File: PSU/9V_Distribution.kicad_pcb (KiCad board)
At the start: 2 copper layers, 50 x 70 mm, 22 parts, among them J1 Screw_Terminal_2_P5.00mm, J2 Screw_Terminal_2_P5.00mm, J3 Screw_Terminal_2_P5.00mm, J4 Screw_Terminal_2_P5.00mm, U4 LM2596S-5

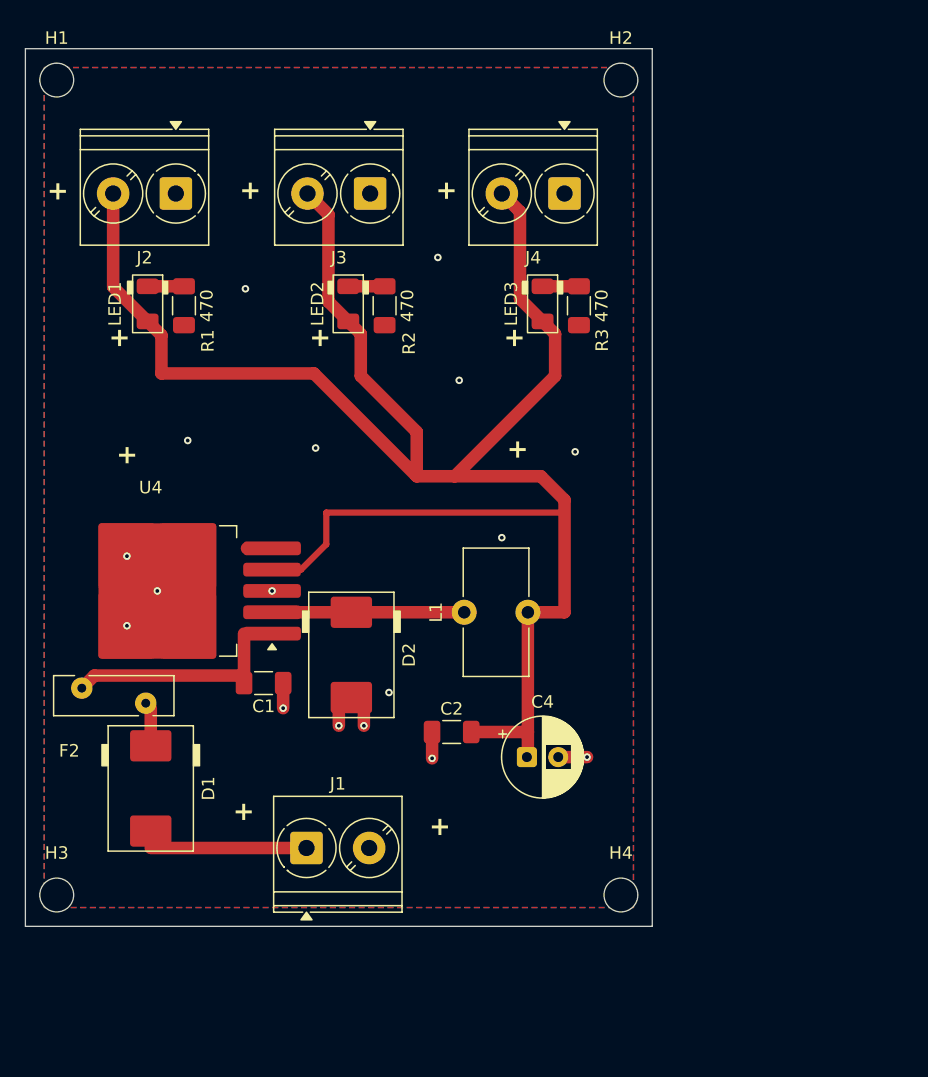
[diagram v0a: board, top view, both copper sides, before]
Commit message: Add the mainboard 9V branch to the PSU
Second, independent regulator on the PSU so the mainboard does not share a
rail with the PWM-switched backlighting. Tapped from D1's cathode: the
reverse protection is shared, the fuse is not, so a fault on one branch
does not take down the other.

  F3  0.5A polyfuse, mainboard branch only
  U1  P78A05-1000, the same module already used on RMP V5
  C5/C6, C7/C8  100nF + 100uF each side, mirroring RMP V5
  J5  screw terminal, beside J1, so both cables leave the same edge

Nets are labelled VIN_MB and +5V_MB rather than left as Net-(U1-+VOUT).

Layout: the whole chain sits in the y 44..56 band, which was empty. That
band was empty of footprints but not of copper -- the buck's output
distribution ran through it to reach J2/J3/J4. That distribution now runs
on a spine above the band at y 44.8 and crosses to the bottom half through
a single 13mm bottom-layer link at x 144.5, well away from the switching
loop. Everything else stays on the front, so the ground plane keeps one
narrow slot and nothing more.

The 9V climbs the left edge in the 2mm corridor between the board edge and
U4's tab; the 5V descends the right edge to J5. C4 moved 1.5mm to clear
the terminal.

0 unconnected items, 0 schematic parity issues, no silkscreen violations.
DRC reports the stale ground pour until the zone is refilled in Pcbnew:
79 of the 95 violations name it, the other 16 are the pre-existing library
links.

Co-Authored-By: Claude Opus 5 <noreply@anthropic.com>
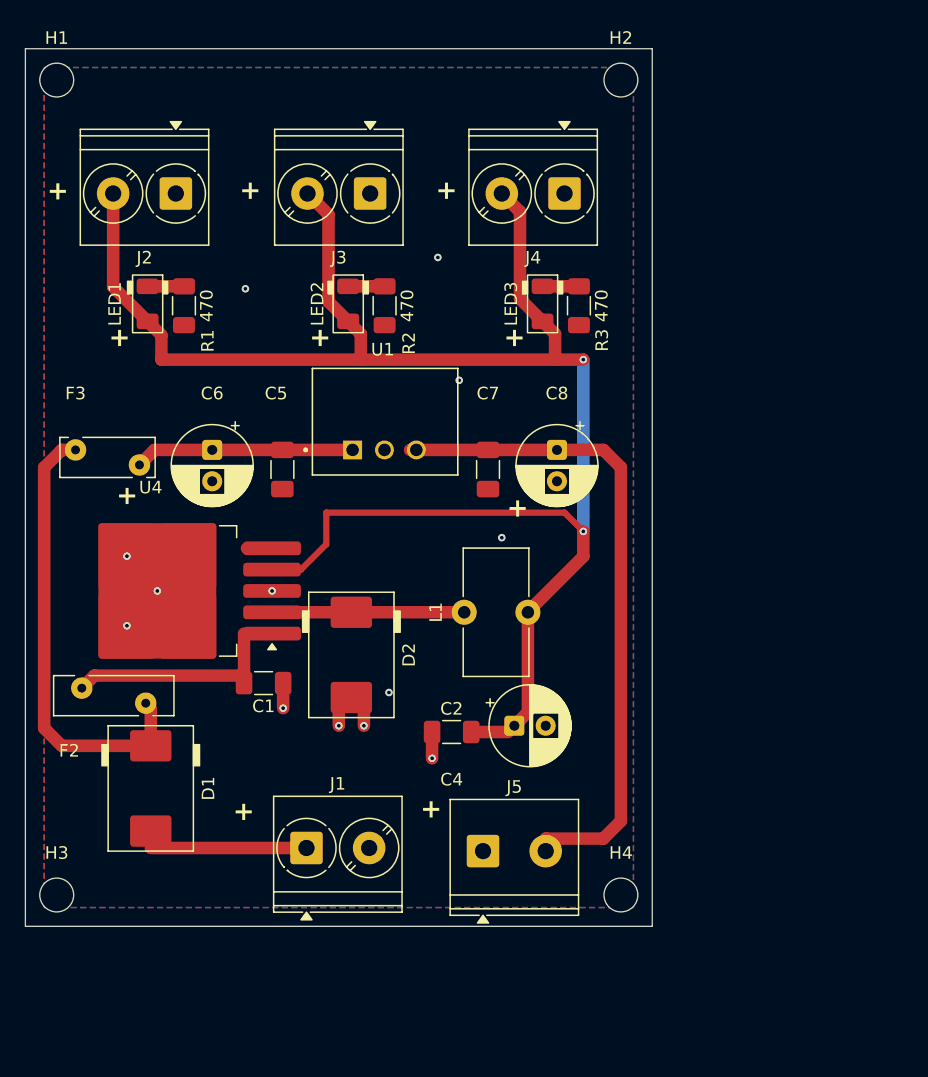
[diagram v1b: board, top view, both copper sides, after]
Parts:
- added C5: 100nF, Capacitor_SMD:C_1206_3216Metric_Pad1.33x1.80mm_HandSolder, F.Cu at (120.5, 53.6)
- added C6: 100uF, Capacitor_THT:CP_Radial_D6.3mm_P2.50mm, F.Cu at (114.9, 52.0)
- added C7: 100nF, Capacitor_SMD:C_1206_3216Metric_Pad1.33x1.80mm_HandSolder, F.Cu at (136.9, 53.6)
- added C8: 100uF, Capacitor_THT:CP_Radial_D6.3mm_P2.50mm, F.Cu at (142.4, 52.0)
- added F3: 0.5A, Fuse:Fuse_Bourns_MF-RHT050, F.Cu at (104.0, 52.0)
- added J5: Screw_Terminal_2_P5.00mm, TerminalBlock_Phoenix:TerminalBlock_Phoenix_PT-1,5-2-5.0-H_1x02_P5.00mm_Horizontal, F.Cu at (136.5, 84.0)
- added U1: P78A05-1000, Custom_Footprints:CONV_P78A05-1000, F.Cu at (126.1, 52.0)
- moved C4 2.69 mm to (139.0, 74.0)
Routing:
- net /+5V_MB: track 0.00 -> 53.2 mm
- net Net-(D1-K): track 3.00 -> 36.0 mm
- net Net-(LED1-A): track 160.7 -> 141.7 mm, vias 0 -> 2
- net /VIN_MB: track 0.00 -> 17.5 mm
- net GND: track 10.5 -> 8.20 mm, vias 17 -> 13

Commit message: Enlarge the PSU to 70x80 and move the mainboard branch into the new space
The board was 50x70 with one regulator; adding a second made it cramped
enough that parts were clearing each other by fractions of a millimetre and
the buck's output had to cross the new chain on the bottom layer.

Growing right and down to 70 x 80 keeps every existing coordinate, so the
buck section does not move. The P78A05 chain now runs vertically in the new
strip at x 150..170, which frees the middle band again: the buck's output
distribution is back to its original routing and the bottom-layer jumper is
gone. All 55 tracks are on the front and the ground plane is uncut.

Mounting holes move to a 65 x 75 pattern, so the printed base needs
reprinting. The 9 V reaches the new strip along the bottom edge at y 78,
between C4's pads and J1's courtyard.

Stitching vias restored in the middle band and added in the new area.

0 schematic parity issues. With the zone fill stripped, DRC finds no
clearance, crossing, short, hole or silkscreen violations; everything it
reports on the file as committed is either the stale pour (23) or the
pre-existing library links (16). Refill in Pcbnew with B.

Co-Authored-By: Claude Opus 5 <noreply@anthropic.com>
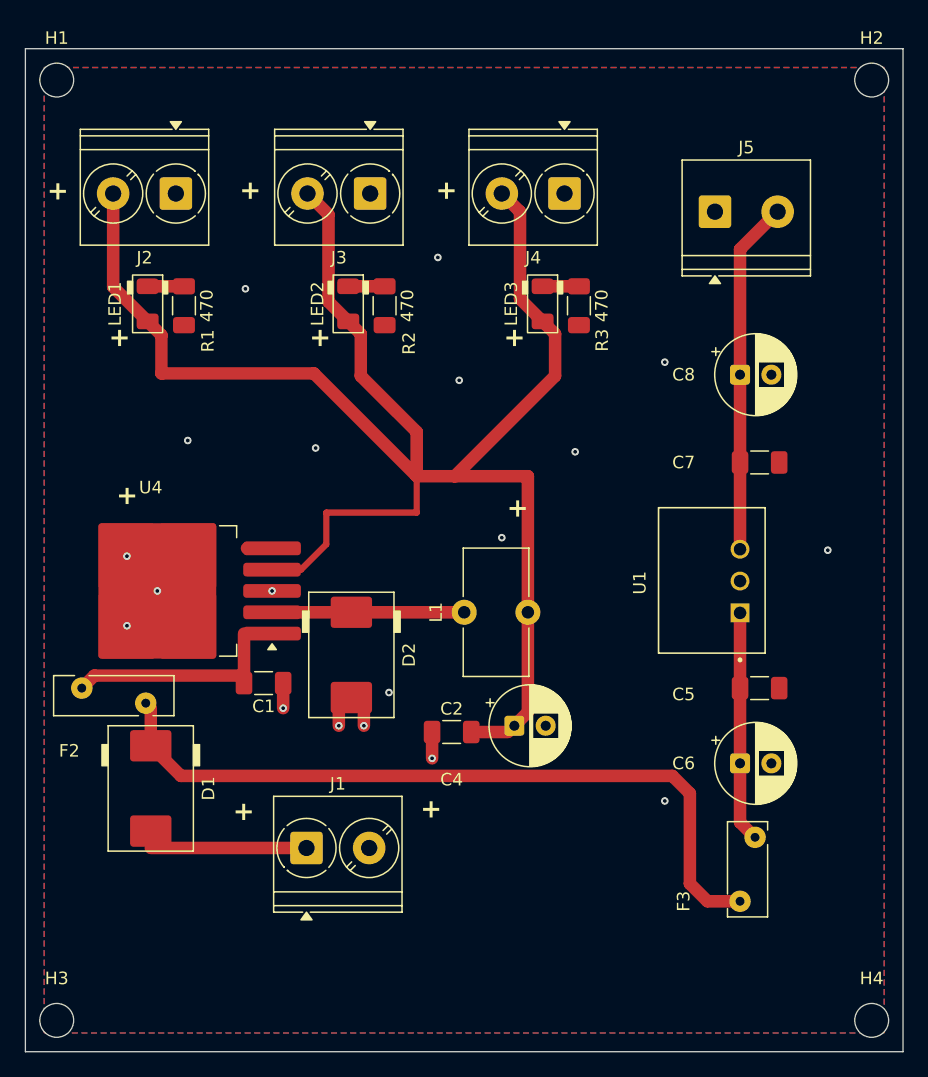
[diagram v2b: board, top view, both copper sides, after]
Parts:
- moved F3 64.1 mm to (157.0, 88.0), turned to 90 degrees
- moved J5 54.3 mm to (155.0, 33.0)
- moved C6 49.0 mm to (157.0, 77.0), turned to 0 degrees
- moved C5 41.9 mm to (158.6, 71.0), turned to 0 degrees
- moved U1 33.5 mm to (157.0, 65.0), turned to 90 degrees
- moved H4 22.4 mm to (167.5, 97.5)
- moved C7 21.7 mm to (158.6, 53.0), turned to 0 degrees
- moved H2 20.0 mm to (167.5, 22.5)
- moved C8 15.8 mm to (157.0, 46.0), turned to 0 degrees
- moved H3 10.0 mm to (102.5, 97.5)
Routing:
- net /+5V_MB: track 53.2 -> 28.2 mm
- net Net-(D1-K): track 36.0 -> 59.4 mm
- net Net-(LED1-A): track 141.7 -> 143.4 mm, vias 2 -> 0
- net /VIN_MB: track 17.5 -> 18.4 mm
- net GND: vias 13 -> 19
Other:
- board size 50 x 70 mm -> 70 x 80 mm

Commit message: Turn J5 round and move the PSU notes clear of the drawing
J5 was placed with its wire entry facing C8, leaving no room for the
cables. Rotated 180 and moved to (160, 33) so the cables leave over the
top edge, the same way J2-J4 do. The output track follows pad 2 to its new
position.

The two schematic notes sat on top of each other and over U1's fields.
They move below the drawing, which ends at y 127, and become four:
the two supply branches, the shared reverse protection with separate
fuses, what D2 is for, and C1's voltage rating. The old note claimed C2
needed 25 V as well; it does not, it sits on the 5 V output.

Includes the zone refill done in Pcbnew, which brought the board to 16
violations, all library links, with 0 unconnected and 0 parity issues.
Moving J5 makes the pour stale again for 8 of them, so it needs one more
refill.

Co-Authored-By: Claude Opus 5 <noreply@anthropic.com>
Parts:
- moved J5 5.00 mm to (160.0, 33.0), turned to 180 degrees

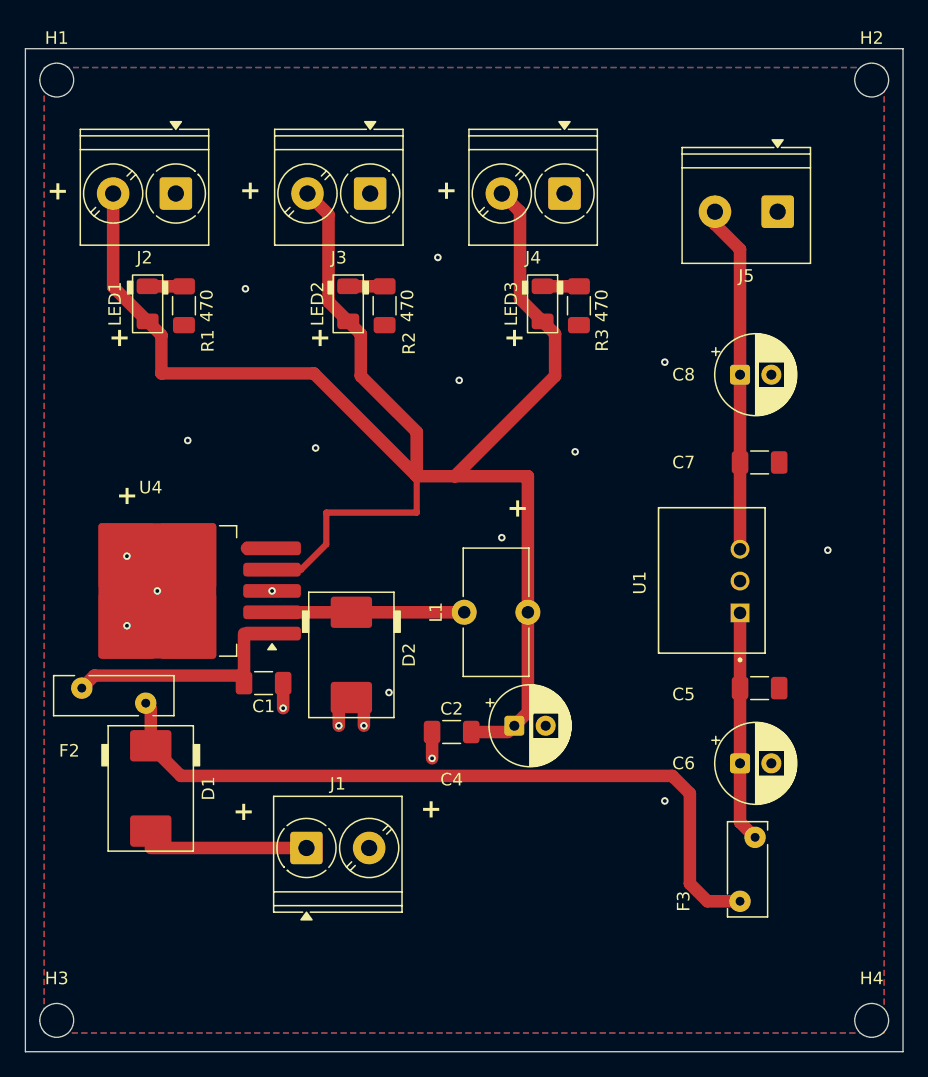
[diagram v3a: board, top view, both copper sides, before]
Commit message: Make the PSU buck section through-hole and give it room
D1, D2, C1 and C2 were SMD in among through-hole parts, for no better reason
than matching what the board already had. Two of the four conversions are
not about convenience:

  C1  sits across the 9V input and needs 25V of rating, which a 1206 MLCC of
      that capacitance does not come in. As an electrolytic the problem goes
      away instead of being documented.
  C2  is the buck's output capacitor and the LM2596 wants ESR there. As a
      ceramic it had none, which is why C4 exists; as an electrolytic it
      brings its own.

D1 and D2 become 1N5822 on the stock Device:D_Schottky symbol, which also
drops four missing-library warnings. Watch the polarity: the SS54 symbol has
pin 1 on the right and D_Schottky has it on the left, so both diodes are
rotated 180 to keep the cathode where it was -- the netlist confirms D1.2 on
the input, D2.1 on the switch node. D2 is mounted vertically on a 5.08mm
pitch, shorter than the SMC's 6.8mm, so the commutation loop tightened.

Side effect worth having: every ground pad in the buck section is now
through-hole and reaches both planes by itself, so four stitching vias and
their stubs are gone.

The whole section is re-placed and re-routed with room to work in, and the
P78A05 strip re-spaced to match. Nothing placed by hand is closer than 2mm
to its neighbour; the tightest pairs left are the original LED-and-resistor
pairs at 0.66mm.

0 unconnected items, 0 schematic parity issues. ERC is down from 15 to 11.
With the fill stripped there are no clearance, crossing, short or silkscreen
violations; 126 of the 138 the file reports are the stale pour and the other
12 are library links. Needs a refill in Pcbnew.

Co-Authored-By: Claude Opus 5 <noreply@anthropic.com>
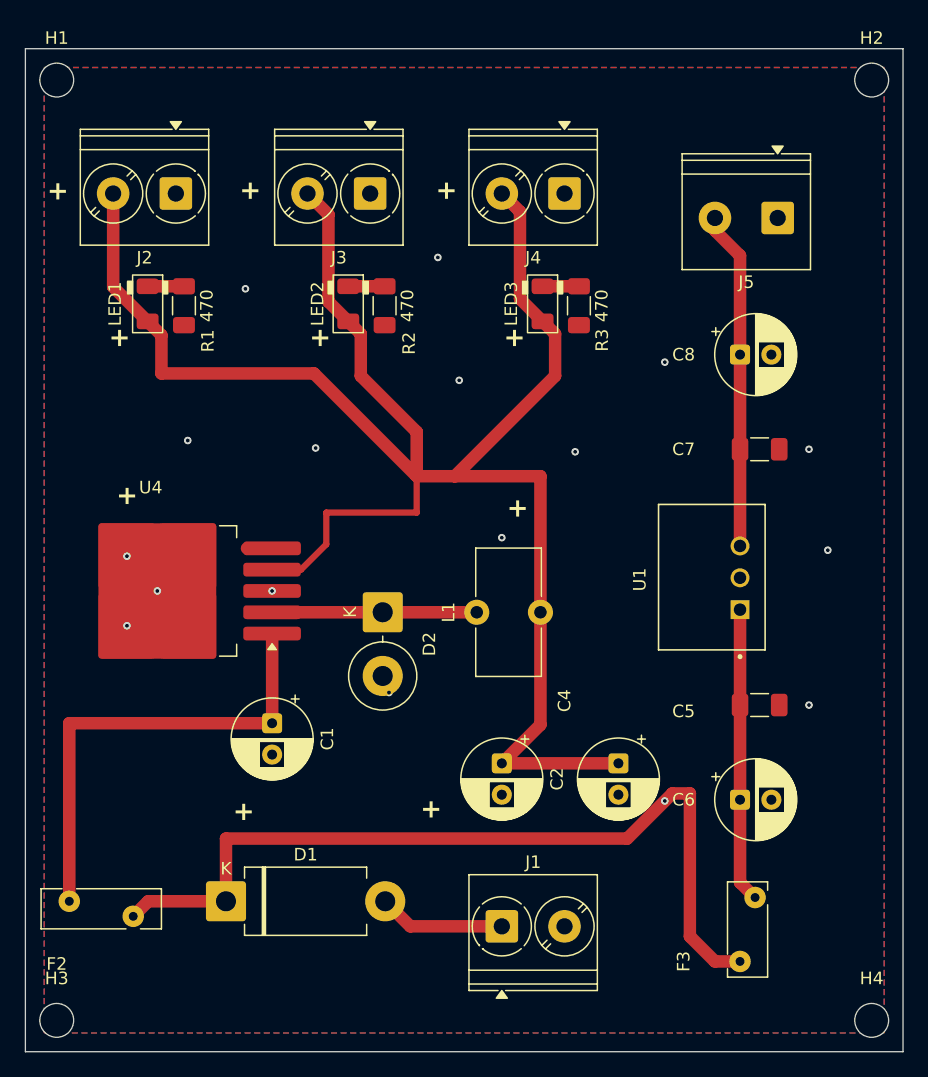
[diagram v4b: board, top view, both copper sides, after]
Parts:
- C1: value 100uF -> 100uF/25V; footprint Capacitor_SMD:C_1206_3216Metric_Pad1.33x1.80mm_HandSolder -> Capacitor_THT:CP_Radial_D6.3mm_P2.50mm
- C2: value 220uF -> 220uF/16V; footprint Capacitor_SMD:C_1206_3216Metric_Pad1.33x1.80mm_HandSolder -> Capacitor_THT:CP_Radial_D6.3mm_P2.50mm
- D1: value SS54 -> 1N5822; footprint PCM_Diode_SMD_AKL:D_SMC -> Diode_THT:D_DO-201AD_P12.70mm_Horizontal
- D2: value SS54 -> 1N5822; footprint PCM_Diode_SMD_AKL:D_SMC -> Diode_THT:D_DO-201AD_P5.08mm_Vertical_CathodeUp
- moved F2 17.0 mm to (103.5, 88.0)
- moved J1 16.8 mm to (138.0, 90.0)
- moved D1 10.8 mm to (116.0, 88.0), turned to 0 degrees
- moved C4 8.83 mm to (147.3, 77.0), turned to 270 degrees
- moved F3 4.80 mm to (157.0, 92.8)
- moved C2 4.72 mm to (138.0, 77.0), turned to 270 degrees
- moved D2 4.22 mm to (128.5, 65.0)
- moved C1 3.27 mm to (119.7, 73.8), turned to 270 degrees
- moved C6 2.90 mm to (157.0, 79.9)
- moved C8 1.60 mm to (157.0, 44.4)
- moved C5 1.35 mm to (158.6, 72.3)
- moved C7 1.05 mm to (158.6, 52.0)
- moved L1 1.00 mm to (136.0, 65.0)
- moved J5 0.50 mm to (160.0, 33.5)
- moved U1 0.26 mm to (157.0, 64.7)
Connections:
- C1 pad 1: GND -> Net-(U4-VIN)
- C1 pad 2: Net-(U4-VIN) -> GND
- C2 pad 1: GND -> Net-(LED1-A)
- C2 pad 2: Net-(LED1-A) -> GND
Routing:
- net Net-(U4-VIN): track 16.7 -> 37.5 mm
- net Net-(LED1-A): track 143.4 -> 154.6 mm
- net Net-(D1-K): track 59.4 -> 67.6 mm
- net GND: track 8.20 -> 2.00 mm, vias 19 -> 17
- net /VIN_MB: track 18.4 -> 23.5 mm
- net Net-(D1-A): track 12.4 -> 10.1 mm
- net Net-(D2-K): track 15.3 -> 16.3 mm
- net /+5V_MB: track 27.7 -> 27.0 mm
